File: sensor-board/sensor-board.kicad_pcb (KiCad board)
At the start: 4 copper layers, 23.4 x 72.3 mm, 102 parts, among them J1 USB_C_Receptacle_USB2.0_16P, J10 cap3, J11 cap4, J2 Conn_01x06, J3 aux pwr, J4 SWD, J5 water 1, J6 water 2, J7 relay, J8 cap1, J9 cap2, K1 SIL03-1A72-71D, Q1 Si2312, Q2 Si2312, SW1 SW_Push, U1 MLPF-WB55-01E3, U10 EKMB130711, U11 DRV5032, U2 STM32WB55CCUx, U3 MCP1703Ax-300xxTT, U4 SHT40-AD1F-R2, U5 VL53L1CXV0FY1, U6 TLV4082, U7 CLS16D24-44, U8 LIS2DE12TR, U9 FDC2114RGHR, Y1 32MHz, Y2 32.768KHz

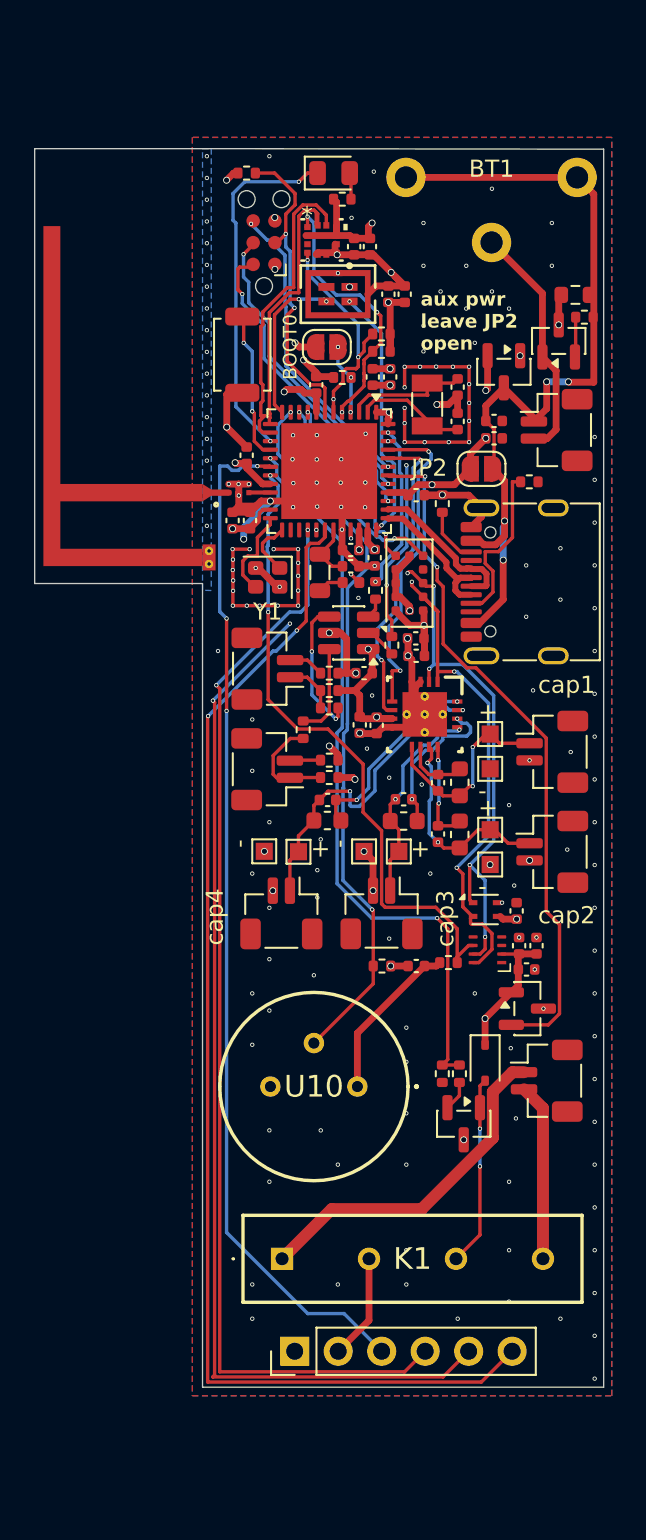
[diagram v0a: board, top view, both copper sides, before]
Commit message: jlcpcb (rotated wrong)
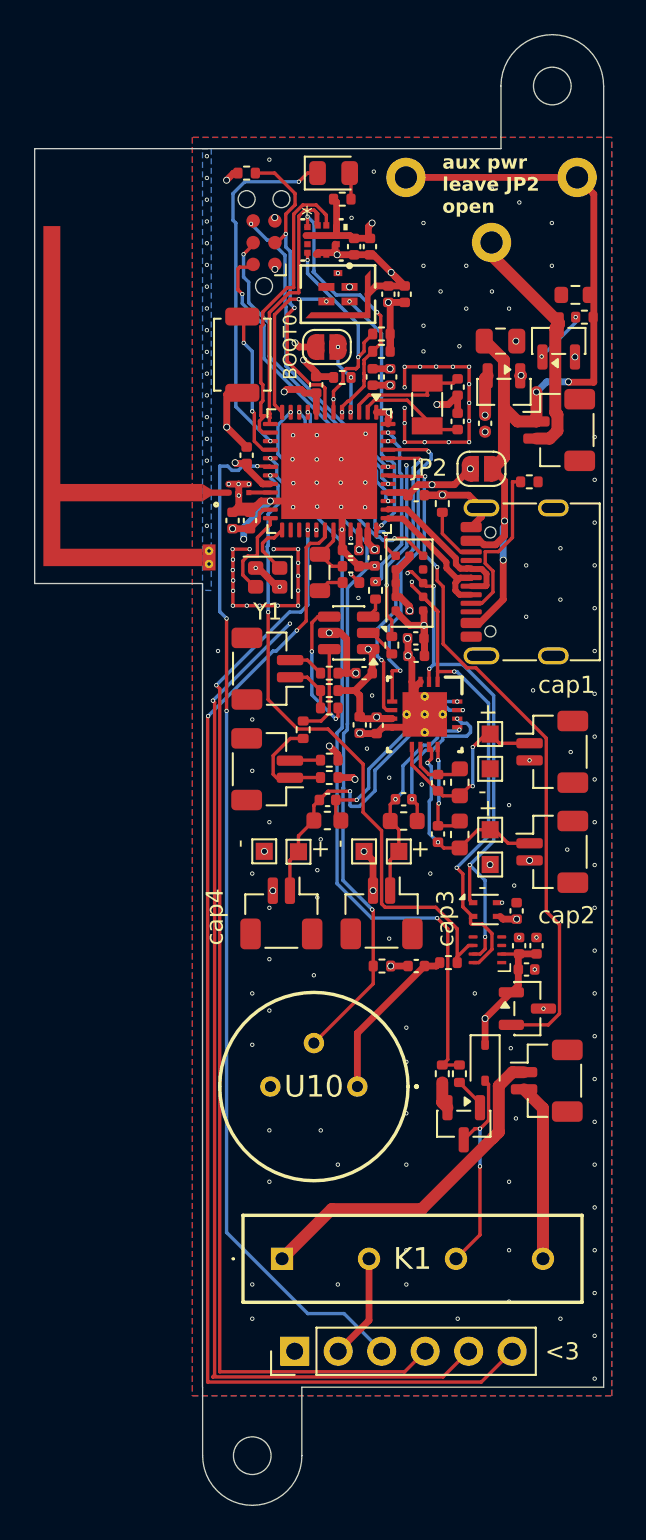
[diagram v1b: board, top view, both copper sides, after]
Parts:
- added H1: MountingHole, MountingHole:MountingHole_2.2mm_M2, F.Cu at (187.5, 32.0)
- added H2: MountingHole, MountingHole:MountingHole_2.2mm_M2, F.Cu at (170.0, 112.0)
- C11: value 4.7uf -> 4.7uF; footprint Capacitor_SMD:C_0402_1005Metric -> Capacitor_SMD:C_0805_2012Metric
- C13: value 4.7uf -> 4.7uF
- moved C11 4.68 mm to (184.5, 46.9)
- moved U3 1.17 mm to (184.7, 49.9)
- moved C13 1.02 mm to (183.6, 51.7), turned to -90 degrees
- moved J3 0.15 mm to (187.9, 52.1)
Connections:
- Q1 pad 1: Net-(BT1--) -> Net-(Q1-G)
- Q1 pad 2: Net-(Q1-G) -> GND
- Q1 pad 3: GND -> Net-(BT1--)
- Q2 pad 1: Net-(D2-A) -> Net-(Q2-D)
- Q2 pad 2: Net-(Q2-G) -> GND
- Q2 pad 3: GND -> Net-(D2-A)
- R12 pad 2: Net-(Q2-G) -> Net-(Q2-D)
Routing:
- net +3V0: track 84.6 -> 80.0 mm
- net Net-(BT1-+): track 49.4 -> 51.7 mm
- net Net-(Q2-D): track 0.00 -> 1.97 mm
- net Net-(Q2-G): track 1.76 -> 0.00 mm
- net Net-(D2-A): track 11.1 -> 12.5 mm
- net Net-(Q1-G): track 2.34 -> 3.18 mm, vias 0 -> 2
- net GND: track 79.6 -> 79.5 mm, vias 193 -> 195
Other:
- board size 23.4 x 72.3 mm -> 23.4 x 85.9 mm
- board text added: "<3"
- board text added: "splurcuit blorb"
- board text added: "thank you dan foisy"
- board text added: "with <3 by aspen and nausicaa"

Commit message: prepare production files
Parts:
- C8: value 1.0uF -> 1uF
- R1: value 1K -> 1k
- R12, R19: value 1.0k -> 1k
- R3, R9: value 10K -> 10k
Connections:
- Y1 pad 4: GND -> (no net)

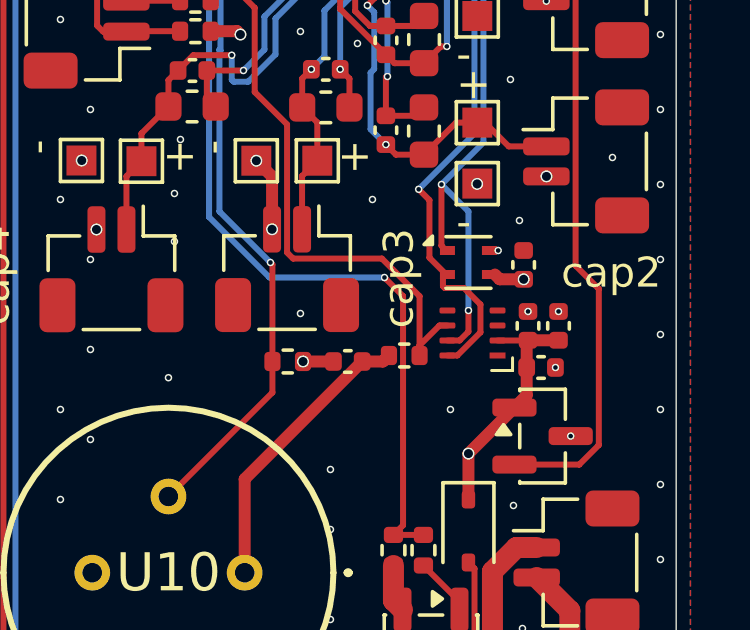
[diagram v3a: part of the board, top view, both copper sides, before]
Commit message: Fix pin numbering for color sensor
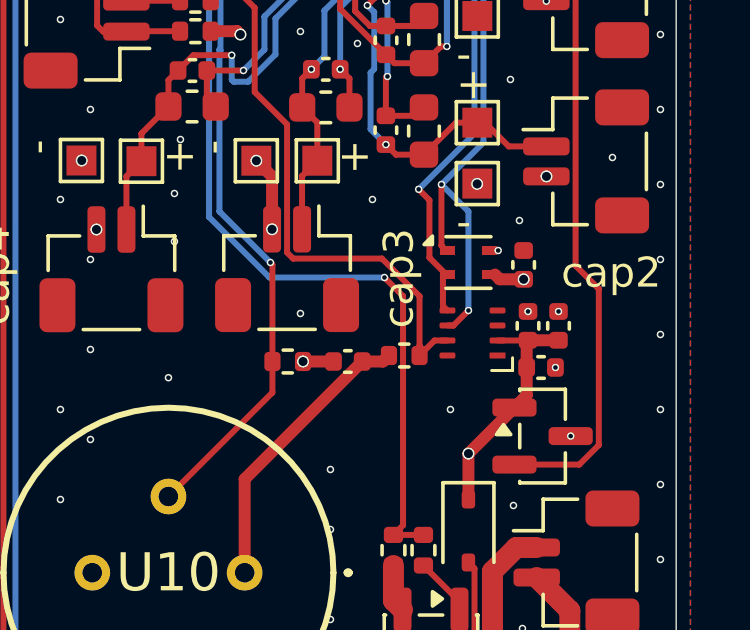
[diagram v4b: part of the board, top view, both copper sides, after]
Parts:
- C8: value 1uF -> 1.0uF
- R1: value 1k -> 1K
- R12, R19: value 1k -> 1.0k
- R3, R9: value 10k -> 10K
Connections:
- Y1 pad 4: (no net) -> GND
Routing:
- net scl: track 56.9 -> 54.0 mm
- net sda: track 56.2 -> 55.6 mm
